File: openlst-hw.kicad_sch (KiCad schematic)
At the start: 4 parts

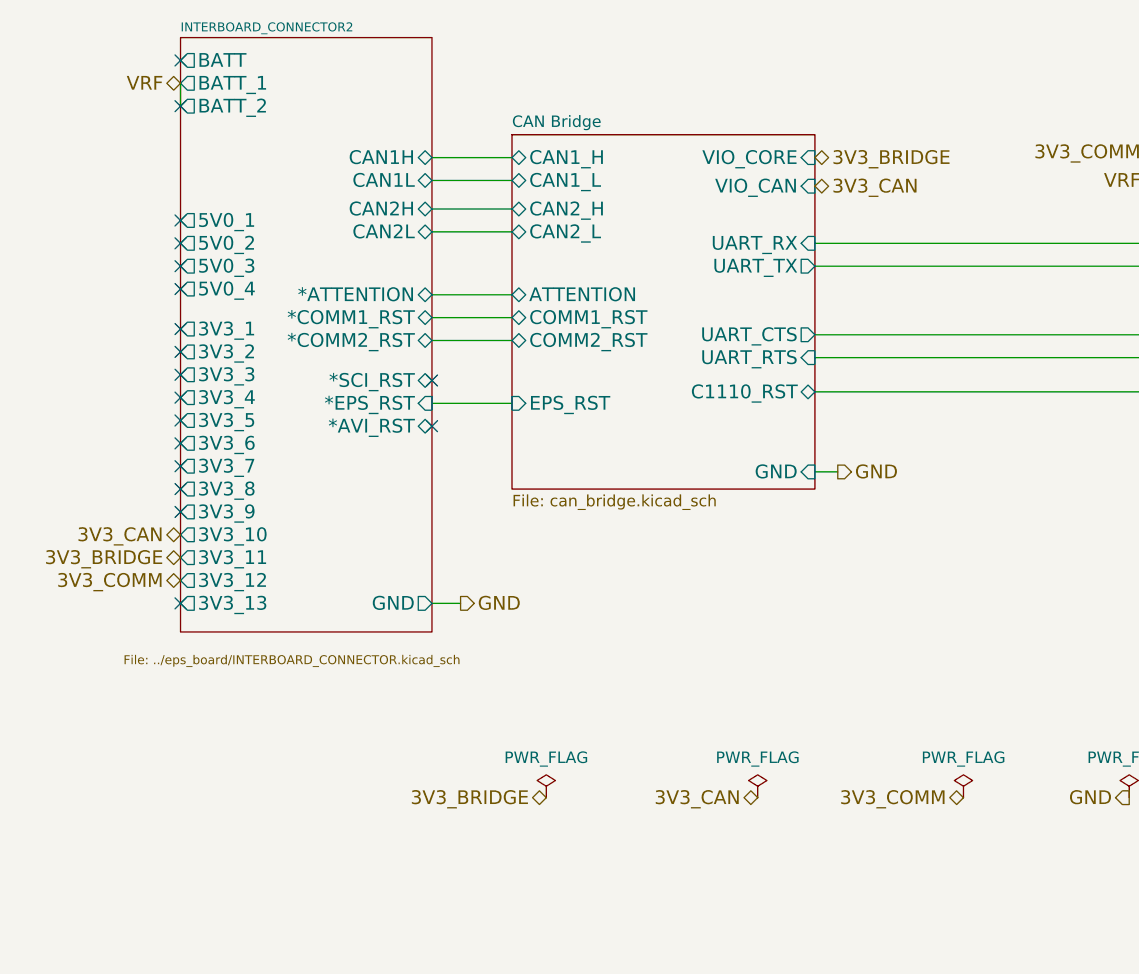
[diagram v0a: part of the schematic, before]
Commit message: openlst board to updated pc104 layout
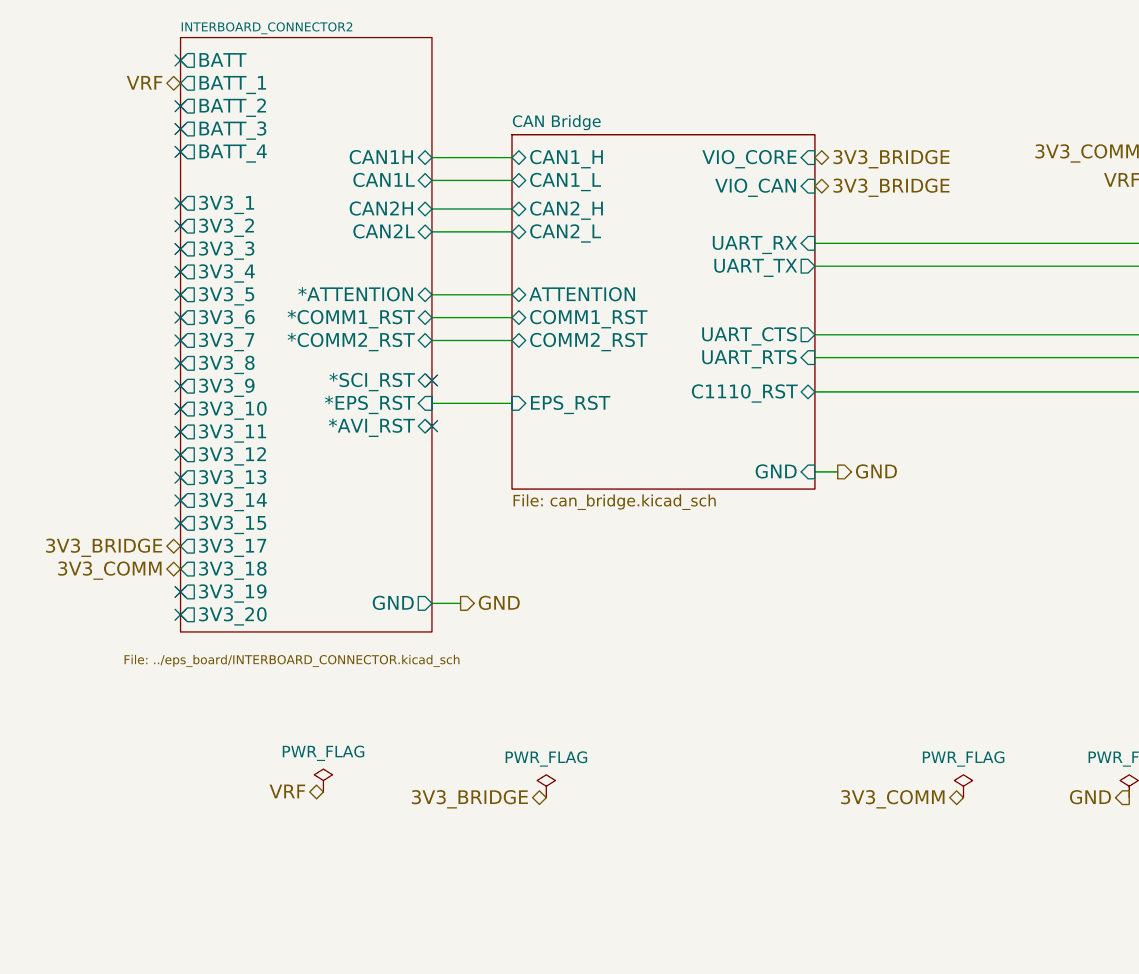
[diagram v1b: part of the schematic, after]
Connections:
- no-connect marks 18 -> 23
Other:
- sheet INTERBOARD_CONNECTOR2 ports: added 3V3_14, 3V3_15, 3V3_17, 3V3_18, 3V3_19, 3V3_20, BATT_3, BATT_4; removed 5V0_1, 5V0_2, 5V0_3, 5V0_4
